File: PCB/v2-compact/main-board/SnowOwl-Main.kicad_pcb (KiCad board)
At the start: 4 copper layers, 60 x 85 mm, 1 part, among them J1 STACK_2x10

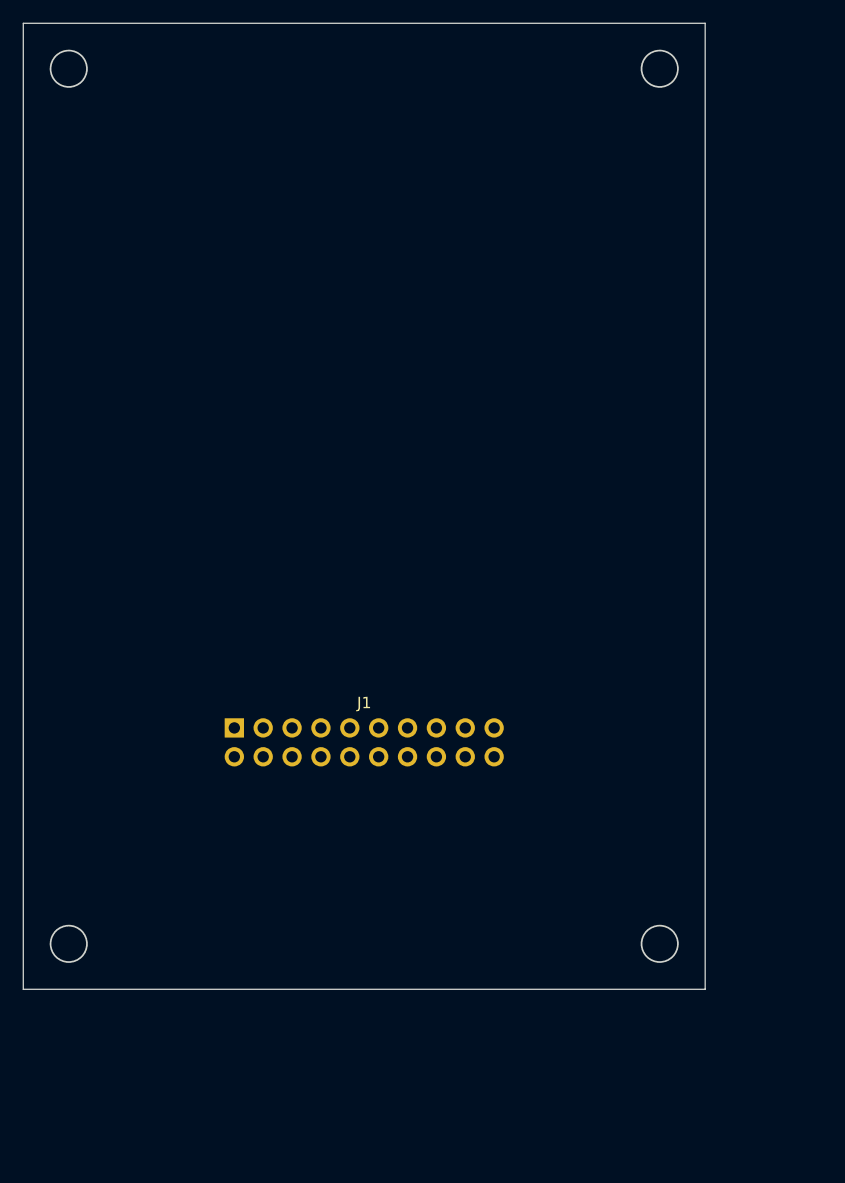
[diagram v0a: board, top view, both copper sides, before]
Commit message: PCB v2: grow to 70x100mm and adopt the C5-owns-radios architecture
Refit the outline to 70x100 after a footprint fit-check: 60x85 could not hold
the RV1106 SoM plus the C5 and nRF24 modules without cramming, which is what
forces congested traces.

- ESP32-C5 now masters the shield SPI spine; every SPI radio taps off it, so
  the whole radio fan-out stays on the shield next to the C5. The S3 commands
  the C5 over one UART on J1 and no SPI radio line crosses the stack header.
- Reflow both boards' zones for short-trace placement, sized to the real part
  footprints; keep the shared J1 datum (53.57, 106.0) so the boards still stack.
- Lock the J1 pinout: power + I2C(PN532) + S3<->C5 UART + S3<->RV1106 UART +
  IR + 1-Wire, with grounds spread for clean returns.
- Rewrite PLACEMENT.md as the updated contract; refresh the shield schematic
  intent note and both floorplan SVGs.
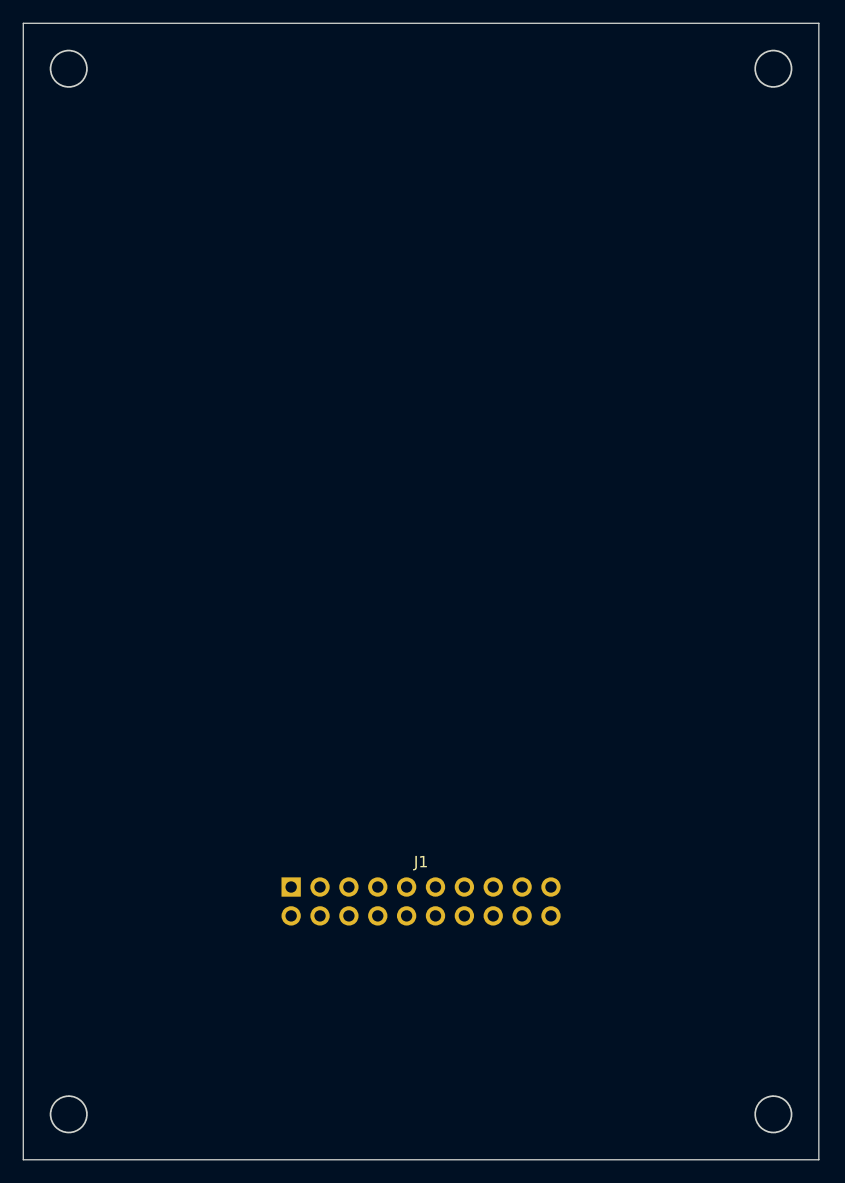
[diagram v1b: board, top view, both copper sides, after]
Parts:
- moved J1 14.9 mm to (53.6, 106.0)
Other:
- board size 60 x 85 mm -> 70 x 100 mm
- board text added: "(BACK) ESP32-S3 (hub)"
- board text added: "(BACK) POWER LDO/ESD"
- board text added: "(BACK) USB-C"
- board text added: "(BACK) microSD"
- board text added: "< uSD (back,E)"
- board text added: "FRONT=UI (User.1) BACK=electronics (User.2) S3 talks to shield over J1 (UART+power)"
- board text added: "NAV BUTTONS"
- board text added: "S3 ANT keepout NW"
- board text added: "TFT DISPLAY (landscape)"
- board text added: "USB-C v (back,S)"
- board text removed: "(BACK) ESP32-S3 (controller/hub)"
- board text removed: "(BACK) POWER (LDO / ESD)"
- board text removed: "(BACK) USB-C (bottom centre)"
- board text removed: "(BACK) microSD (S3)"
- board text removed: "FRONT zones = User.1 BACK zones = User.2 (floorplan skeleton)"
- board text removed: "NAV BUTTONS (moved down)"
- board text removed: "S3 ANT keepout"
- board text removed: "TFT DISPLAY (landscape / sideways)"
- board text removed: "USB-C v (back)"
- board text removed: "uSD > (back)"
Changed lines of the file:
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@@
     (company "YurilLAB")
     (comment 1 "ESP32-SnowOwl v2 - compact 2-board stack")
-    (comment 2 "Floorplan skeleton - deliberate placement, route later")
+    (comment 2 "Floorplan skeleton - 70x100mm, C5 owns shield radios")
   )
   (layers
@@
   )
   (net 0 "")
-  (gr_rect (start 30 30) (end 90 115) (stroke (width 0.1) (type solid)) (fill none) (layer "Edge.Cuts"))
-  (gr_circle (center 34.0 34.0) (end 35.6 34.0) (stroke (width 0.15) (type solid)) (fill none) (layer "Edge.Cuts"))
-  (gr_circle (center 86.0 34.0) (end 87.6 34.0) (stroke (width 0.15) (type solid)) (fill none) (layer "Edge.Cuts"))
-  (gr_circle (center 34.0 111.0) (end 35.6 111.0) (stroke (width 0.15) (type solid)) (fill none) (layer "Edge.Cuts"))
-  (gr_circle (center 86.0 111.0) (end 87.6 111.0) (stroke (width 0.15) (type solid)) (fill none) (layer "Edge.Cuts"))
-  (gr_text "SnowOwl v2 - Main Board" (at 32.0 26.0) (layer "Cmts.User")
-    (effects (font (size 2.0 2.0) (thickness 0.3)) (justify left)))
-  (gr_text "FRONT zones = User.1   BACK zones = User.2   (floorplan skeleton)" (at 32.0 119.0) (layer "Cmts.User")
+  (gr_rect (start 30 30) (end 100 130) (stroke (width 0.1) (type solid)) (fill none) (layer "Edge.Cuts"))
+  (gr_circle (center 34 34) (end 35.6 34) (stroke (width 0.15) (type solid)) (fill none) (layer "Edge.Cuts"))
+  (gr_circle (center 96 34) (end 97.6 34) (stroke (width 0.15) (type solid)) (fill none) (layer "Edge.Cuts"))
+  (gr_circle (center 34 126) (end 35.6 126) (stroke (width 0.15) (type solid)) (fill none) (layer "Edge.Cuts"))
+  (gr_circle (center 96 126) (end 97.6 126) (stroke (width 0.15) (type solid)) (fill none) (layer "Edge.Cuts"))
+  (gr_text "SnowOwl v2 - Main Board" (at 32 26) (layer "Cmts.User")
+    (effects (font (size 2 2) (thickness 0.3)) (justify left)))
+  (gr_text "FRONT=UI (User.1)  BACK=electronics (User.2)   S3 talks to shield over J1 (UART+power)" (at 32 128.5) (layer "Cmts.User")
     (effects (font (size 1.1 1.1) (thickness 0.18)) (justify left)))
-  (gr_rect (start 49.0 33.0) (end 75.0 39.0) (stroke (width 0.15) (type solid)) (fill none) (layer "User.1"))
-  (gr_text "STATUS LEDs" (at 49.8 35.0) (layer "User.1")
+  (gr_rect (start 38 34) (end 92 42) (stroke (width 0.15) (type solid)) (fill none) (layer "User.1"))
+  (gr_text "STATUS LEDs" (at 38.8 36) (layer "User.1")
     (effects (font (size 1.1 1.1) (thickness 0.18)) (justify left)))
-  (gr_rect (start 35.0 41.0) (end 85.0 76.0) (stroke (width 0.15) (type solid)) (fill none) (layer "User.1"))
-  (gr_text "TFT DISPLAY (landscape / sideways)" (at 35.8 43.0) (layer "User.1")
+  (gr_rect (start 36 46) (end 96 86) (stroke (width 0.15) (type solid)) (fill none) (layer "User.1"))
+  (gr_text "TFT DISPLAY (landscape)" (at 36.8 48) (layer "User.1")
     (effects (font (size 1.1 1.1) (thickness 0.18)) (justify left)))
-  (gr_rect (start 47.0 80.0) (end 73.0 89.0) (stroke (width 0.15) (type solid)) (fill none) (layer "User.1"))
-  (gr_text "NAV BUTTONS (moved down)" (at 47.8 82.0) (layer "User.1")
+  (gr_rect (start 46 92) (end 86 104) (stroke (width 0.15) (type solid)) (fill none) (layer "User.1"))
+  (gr_text "NAV BUTTONS" (at 46.8 94) (layer "User.1")
     (effects (font (size 1.1 1.1) (thickness 0.18)) (justify left)))
-  (gr_rect (start 44.0 43.0) (end 72.0 70.0) (stroke (width 0.12) (type solid)) (fill none) (layer "User.2"))
-  (gr_text "(BACK) ESP32-S3 (controller/hub)" (at 44.8 45.0) (layer "User.2")
+  (gr_rect (start 50 44) (end 82 74) (stroke (width 0.12) (type solid)) (fill none) (layer "User.2"))
+  (gr_text "(BACK) ESP32-S3 (hub)" (at 50.8 46) (layer "User.2")
     (effects (font (size 1.1 1.1) (thickness 0.18)) (justify left)))
-  (gr_rect (start 74.0 60.0) (end 87.0 80.0) (stroke (width 0.12) (type solid)) (fill none) (layer "User.2"))
-  (gr_text "(BACK) microSD (S3)" (at 74.8 62.0) (layer "User.2")
+  (gr_rect (start 84 50) (end 98 74) (stroke (width 0.12) (type solid)) (fill none) (layer "User.2"))
+  (gr_text "(BACK) microSD" (at 84.8 52) (layer "User.2")
     (effects (font (size 1.1 1.1) (thickness 0.18)) (justify left)))
-  (gr_rect (start 34.0 92.0) (end 48.0 112.0) (stroke (width 0.12) (type solid)) (fill none) (layer "User.2"))
-  (gr_text "(BACK) POWER (LDO / ESD)" (at 34.8 94.0) (layer "User.2")
+  (gr_rect (start 34 96) (end 54 118) (stroke (width 0.12) (type solid)) (fill none) (layer "User.2"))
+  (gr_text "(BACK) POWER LDO/ESD" (at 34.8 98) (layer "User.2")
     (effects (font (size 1.1 1.1) (thickness 0.18)) (justify left)))
-  (gr_rect (start 53.0 107.0) (end 69.0 114.0) (stroke (width 0.12) (type solid)) (fill none) (layer "User.2"))
-  (gr_text "(BACK) USB-C (bottom centre)" (at 53.8 109.0) (layer "User.2")
+  (gr_rect (start 56 116) (end 76 126) (stroke (width 0.12) (type solid)) (fill none) (layer "User.2"))
+  (gr_text "(BACK) USB-C" (at 56.8 118) (layer "User.2")
     (effects (font (size 1.1 1.1) (thickness 0.18)) (justify left)))
-  (gr_text "S3 ANT keepout" (at 33.5 41.5) (layer "Cmts.User")
-    (effects (font (size 1.0 1.0) (thickness 0.15)) (justify left)))
-  (gr_text "USB-C v (back)" (at 54.0 113.5) (layer "Cmts.User")
-    (effects (font (size 1.0 1.0) (thickness 0.15)) (justify left)))
-  (gr_text "uSD > (back)" (at 87.5 70.0) (layer "Cmts.User")
-    (effects (font (size 1.0 1.0) (thickness 0.15)) (justify left)))
+  (gr_text "S3 ANT keepout NW" (at 31 50) (layer "Cmts.User")
+    (effects (font (size 1 1) (thickness 0.15)) (justify left)))
+  (gr_text "< uSD (back,E)" (at 99 60) (layer "Cmts.User")
+    (effects (font (size 1 1) (thickness 0.15)) (justify left)))
+  (gr_text "USB-C v (back,S)" (at 58 128) (layer "Cmts.User")
+    (effects (font (size 1 1) (thickness 0.15)) (justify left)))
   (footprint "SnowOwl:StackHeader_2x10" (layer "F.Cu")
-    (at 48.57 92.0)
+    (at 53.57 106.00)
     (descr "SnowOwl 2x10 2.54mm inter-board stack header (shared datum)")
     (attr through_hole)
@@
     (fp_text value "STACK_2x10" (at 11.43 4.7) (layer "F.Fab")
       (effects (font (size 1 1) (thickness 0.15))))
-    (pad "1" thru_hole rect (at 0.0 0.0) (size 1.7 1.7) (drill 1.0) (layers "*.Cu" "*.Mask"))
+    (pad "1" thru_hole rect (at 0.00 0.0) (size 1.7 1.7) (drill 1.0) (layers "*.Cu" "*.Mask"))
     (pad "2" thru_hole oval (at 2.54 0.0) (size 1.7 1.7) (drill 1.0) (layers "*.Cu" "*.Mask"))
     (pad "3" thru_hole oval (at 5.08 0.0) (size 1.7 1.7) (drill 1.0) (layers "*.Cu" "*.Mask"))
     (pad "4" thru_hole oval (at 7.62 0.0) (size 1.7 1.7) (drill 1.0) (layers "*.Cu" "*.Mask"))
     (pad "5" thru_hole oval (at 10.16 0.0) (size 1.7 1.7) (drill 1.0) (layers "*.Cu" "*.Mask"))
-    (pad "6" thru_hole oval (at 12.7 0.0) (size 1.7 1.7) (drill 1.0) (layers "*.Cu" "*.Mask"))
+    (pad "6" thru_hole oval (at 12.70 0.0) (size 1.7 1.7) (drill 1.0) (layers "*.Cu" "*.Mask"))
     (pad "7" thru_hole oval (at 15.24 0.0) (size 1.7 1.7) (drill 1.0) (layers "*.Cu" "*.Mask"))
     (pad "8" thru_hole oval (at 17.78 0.0) (size 1.7 1.7) (drill 1.0) (layers "*.Cu" "*.Mask"))
     (pad "9" thru_hole oval (at 20.32 0.0) (size 1.7 1.7) (drill 1.0) (layers "*.Cu" "*.Mask"))
     (pad "10" thru_hole oval (at 22.86 0.0) (size 1.7 1.7) (drill 1.0) (layers "*.Cu" "*.Mask"))
-    (pad "11" thru_hole oval (at 0.0 2.54) (size 1.7 1.7) (drill 1.0) (layers "*.Cu" "*.Mask"))
+    (pad "11" thru_hole oval (at 0.00 2.54) (size 1.7 1.7) (drill 1.0) (layers "*.Cu" "*.Mask"))
     (pad "12" thru_hole oval (at 2.54 2.54) (size 1.7 1.7) (drill 1.0) (layers "*.Cu" "*.Mask"))
     (pad "13" thru_hole oval (at 5.08 2.54) (size 1.7 1.7) (drill 1.0) (layers "*.Cu" "*.Mask"))
     (pad "14" thru_hole oval (at 7.62 2.54) (size 1.7 1.7) (drill 1.0) (layers "*.Cu" "*.Mask"))
     (pad "15" thru_hole oval (at 10.16 2.54) (size 1.7 1.7) (drill 1.0) (layers "*.Cu" "*.Mask"))
-    (pad "16" thru_hole oval (at 12.7 2.54) (size 1.7 1.7) (drill 1.0) (layers "*.Cu" "*.Mask"))
+    (pad "16" thru_hole oval (at 12.70 2.54) (size 1.7 1.7) (drill 1.0) (layers "*.Cu" "*.Mask"))
     (pad "17" thru_hole oval (at 15.24 2.54) (size 1.7 1.7) (drill 1.0) (layers "*.Cu" "*.Mask"))
     (pad "18" thru_hole oval (at 17.78 2.54) (size 1.7 1.7) (drill 1.0) (layers "*.Cu" "*.Mask"))
@@
     (pad "20" thru_hole oval (at 22.86 2.54) (size 1.7 1.7) (drill 1.0) (layers "*.Cu" "*.Mask"))
   )
-  (gr_text "J1 STACK (datum: shared X/Y on both boards)" (at 48.57 97.0) (layer "Cmts.User")
-    (effects (font (size 1.0 1.0) (thickness 0.15)) (justify left)))
+  (gr_text "J1 STACK (datum: shared X/Y on both boards)" (at 53.57 111) (layer "Cmts.User")
+    (effects (font (size 1 1) (thickness 0.15)) (justify left)))
 )

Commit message: PCB: import schematic netlists onto both boards (parts placed + nets assigned)
Load every footprint from the schematic into the floorplan-skeleton boards,
place each in its subsystem's zone (grid-spread, back-side sheets flipped), and
assign all nets. Shield: 79 parts, 419 pad-nets, 153 nets. Main: 29 parts,
150 pad-nets, 57 nets. Register the Espressif footprint library; add a
placeholder Core1106 SoM footprint; assign the C5 (Espressif), NEO-M9N (ublox_NEO)
and CC1101 (2x4 header) module footprints.

This is the initial import: every part is on its board with the full ratsnest,
ready for placement refinement and routing.
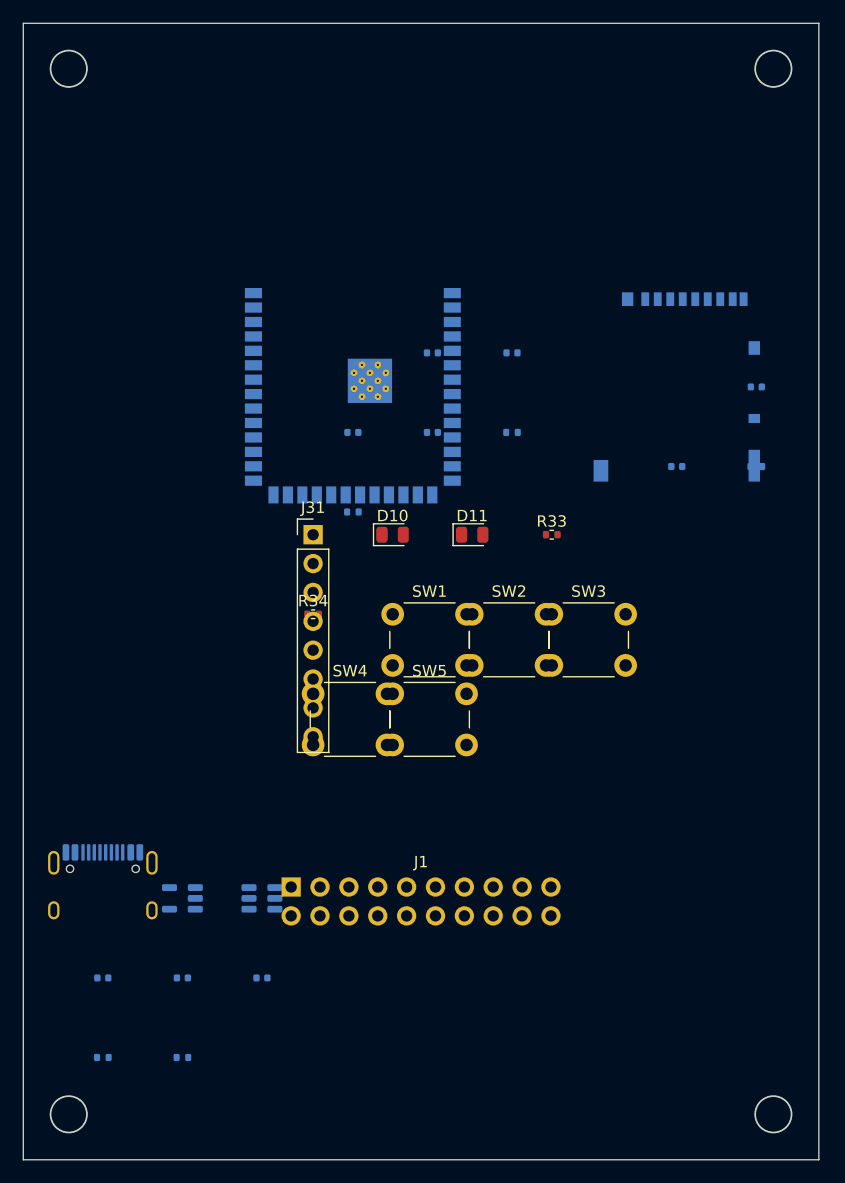
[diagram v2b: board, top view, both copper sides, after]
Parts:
- added C20: 10uF, C_0402_1005Metric, B.Cu at (37.0, 114.0)
- added C21: 10uF, C_0402_1005Metric, B.Cu at (44.0, 114.0)
- added C22: 100nF, C_0402_1005Metric, B.Cu at (51.0, 114.0)
- added C30: 10uF, C_0402_1005Metric, B.Cu at (66.0, 59.0)
- added C31: 100nF, C_0402_1005Metric, B.Cu at (73.0, 59.0)
- added C32: 100nF, C_0402_1005Metric, B.Cu at (59.0, 66.0)
- added C33: 1uF, C_0402_1005Metric, B.Cu at (66.0, 66.0)
- added C34: 100nF, C_0402_1005Metric, B.Cu at (94.5, 62.0)
- added C35: 10uF, C_0402_1005Metric, B.Cu at (87.5, 69.0)
- added D10: GRN, LED_0805_2012Metric, F.Cu at (62.5, 75.0)
- added D11: BLU, LED_0805_2012Metric, F.Cu at (69.5, 75.0)
- added J20: USB-C, USB_C_Receptacle_HRO_TYPE-C-31-M-12, B.Cu at (37.0, 107.0)
- added J30: microSD, microSD_HC_Hirose_DM3AT-SF-PEJM5, B.Cu at (87.5, 62.0)
- added J31: TFT_SPI, PinHeader_1x08_P2.54mm_Vertical, F.Cu at (55.5, 75.0)
- added R20: 5k1, R_0402_1005Metric, B.Cu at (37.0, 121.0)
- added R21: 5k1, R_0402_1005Metric, B.Cu at (44.0, 121.0)
- added R30: 10k, R_0402_1005Metric, B.Cu at (73.0, 66.0)
- added R31: 10k, R_0402_1005Metric, B.Cu at (59.0, 73.0)
- added R32: 10k, R_0402_1005Metric, B.Cu at (94.5, 69.0)
- added R33: 1k, R_0402_1005Metric, F.Cu at (76.5, 75.0)
- added R34: 1k, R_0402_1005Metric, F.Cu at (55.5, 82.0)
- added SW1: BTN_UP, SW_PUSH_6mm, F.Cu at (62.5, 82.0)
- added SW2: BTN_DN, SW_PUSH_6mm, F.Cu at (69.5, 82.0)
- added SW3: BTN_L, SW_PUSH_6mm, F.Cu at (76.5, 82.0)
- added SW4: BTN_R, SW_PUSH_6mm, F.Cu at (55.5, 89.0)
- added SW5: BTN_OK, SW_PUSH_6mm, F.Cu at (62.5, 89.0)
- added U20: ESP32-S3-WROOM-1-N8, ESP32-S3-WROOM-1, B.Cu at (59.0, 59.0)
- added U21: AP7361C-3.3, SOT-23-5, B.Cu at (44.0, 107.0)
- added U22: USBLC6-2SC6, SOT-23-6, B.Cu at (51.0, 107.0)
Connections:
- J1 pad 1: (no net) -> +5V
- J1 pad 10: (no net) -> GND
- J1 pad 11: (no net) -> GND
- J1 pad 12: (no net) -> OW_1WIRE
- J1 pad 13: (no net) -> IR_RX
- J1 pad 14: (no net) -> IR_TX
- J1 pad 15: (no net) -> GND
- J1 pad 16: (no net) -> RV_TX
- J1 pad 17: (no net) -> RV_RX
- J1 pad 18: (no net) -> RV_CTRL
- J1 pad 19: (no net) -> SPARE
- J1 pad 2: (no net) -> +3V3
- J1 pad 20: (no net) -> GND
- J1 pad 3: (no net) -> GND
- J1 pad 4: (no net) -> SDA
- J1 pad 5: (no net) -> SCL
- J1 pad 6: (no net) -> GND
- J1 pad 7: (no net) -> C5_TX
- J1 pad 8: (no net) -> C5_RX
- J1 pad 9: (no net) -> C5_DRDY
